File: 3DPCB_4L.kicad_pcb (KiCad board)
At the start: 4 copper layers, 100 x 60 mm, 777 parts, among them IC1 A5984_LP, IC2 A5984_LP, IC3 A5984_LP, IC4 A5984_LP, IC5 A5984_LP, IC6 MP9943, J10 , J11 , J12 , J13 , J14 , J15 , J16 , J2 , J3 , J4 , J5 , J6 , J7 , J8 , J9 , K1 CONN_3, K2 CONN_3, K3 CONN_3, K4 CONN_3, K5 CONN_3, K6 CONN_3, K7 CONN_3, K8 CONN_3, K9 CONN_3, P1 CONN_8, P11 CONN_3X2, P12 CONN_3X2, P13 CONN_4, P2 CONN_8, P5 CONN_4, P6 CONN_4, P7 CONN_4, P8 CONN_02X03, P9 CONN_4, U1 CONN_4_LERCHE, U10 MICRO-SD, U11 TC4427, U12 MCP4728, U13 CONN_4_LERCHE, U15 SPST_MOMENTARY, U16 CONN_4_LERCHE, U2 SPST_MOMENTARY, U21 CONN_4_LERCHE, U22 CONN_4_LERCHE, U23 MCP4728, U24 IRFH5302, U25 CONN_4_LERCHE, U3 BSS84, U4 CONN_4_LERCHE, U5 IRFH5302, U6 LPC1768_TQFP100, U7 IRFH5302, U8 IRFH5302, U9 TC4427

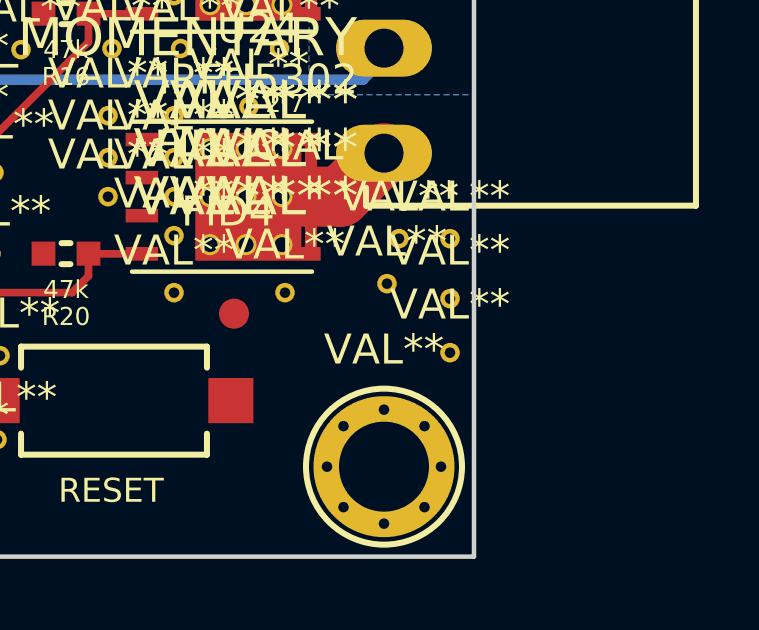
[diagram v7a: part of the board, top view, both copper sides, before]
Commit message: Spokes on high current path removed.
Spokes on high current path removed.
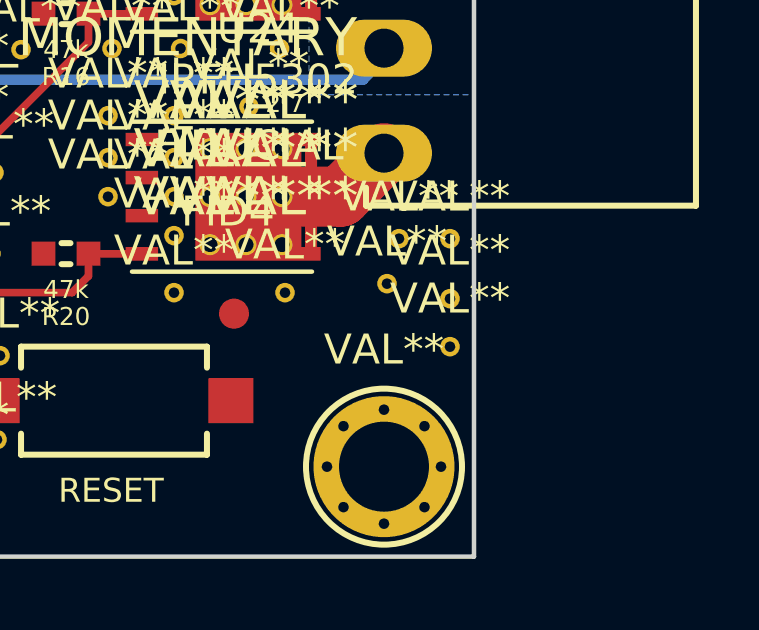
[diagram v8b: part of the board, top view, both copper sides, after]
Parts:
- moved ? 0.20 mm to (229.2, 188.5)
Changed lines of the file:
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@@
     (links 1072)
     (no_connects 0)
-    (area 129.924999 135.424999 230.075001 195.575001)
+    (area 126.046317 131.0284 237.651491 200.475)
     (thickness 1.6)
     (drawings 131)
@@
   (layers
     (0 F.Cu mixed)
-    (1 Inner2.Cu power)
-    (2 Inner1.Cu power)
+    (1 Inner2.Cu power hide)
+    (2 Inner1.Cu power hide)
     (31 B.Cu mixed)
     (32 B.Adhes user)
@@
     (mod_text_size 1 1)
     (mod_text_width 0.15)
-    (pad_size 4.32 3)
+    (pad_size 1.25 1.8)
     (pad_drill 0)
     (pad_to_mask_clearance 0)
@@
   )
   (module Lerche_via_0.35_GND (layer F.Cu)
-    (at 229.2 188.7)
+    (at 229.2 188.5)
     (fp_text reference "" (at 0 -3.2) (layer F.SilkS)
       (effects (font (size 1 1) (thickness 0.15)))
@@
       (net 171 "Net-(IC1-Pad17)"))
     (pad 2 smd rect (at 1.4 0) (size 1.25 1.8) (layers F.Cu F.Paste F.Mask)
-      (net 19 GND))
+      (net 19 GND) (zone_connect 2))
     (model Resistors_SMD.3dshapes/R_1206.wrl
       (at (xyz 0 0 0))
@@
       (net 173 "Net-(IC1-Pad20)"))
     (pad 2 smd rect (at 1.4 0 180) (size 1.25 1.8) (layers F.Cu F.Paste F.Mask)
-      (net 19 GND))
+      (net 19 GND) (zone_connect 2))
     (model Resistors_SMD.3dshapes/R_1206.wrl
       (at (xyz 0 0 0))
@@
       (net 195 "Net-(IC5-Pad17)"))
     (pad 2 smd rect (at 1.4 0) (size 1.25 1.8) (layers F.Cu F.Paste F.Mask)
-      (net 19 GND))
+      (net 19 GND) (zone_connect 2))
     (model Resistors_SMD.3dshapes/R_1206.wrl
       (at (xyz 0 0 0))
@@
       (net 197 "Net-(IC5-Pad20)"))
     (pad 2 smd rect (at 1.4 0 180) (size 1.25 1.8) (layers F.Cu F.Paste F.Mask)
-      (net 19 GND))
+      (net 19 GND) (zone_connect 2))
     (model Resistors_SMD.3dshapes/R_1206.wrl
       (at (xyz 0 0 0))
@@
       (net 189 "Net-(IC4-Pad17)"))
     (pad 2 smd rect (at 1.4 0) (size 1.25 1.8) (layers F.Cu F.Paste F.Mask)
-      (net 19 GND))
+      (net 19 GND) (zone_connect 2))
     (model Resistors_SMD.3dshapes/R_1206.wrl
       (at (xyz 0 0 0))
@@
       (net 183 "Net-(IC3-Pad17)"))
     (pad 2 smd rect (at 1.4 0) (size 1.25 1.8) (layers F.Cu F.Paste F.Mask)
-      (net 19 GND))
+      (net 19 GND) (zone_connect 2))
     (model Resistors_SMD.3dshapes/R_1206.wrl
       (at (xyz 0 0 0))
@@
       (net 177 "Net-(IC2-Pad17)"))
     (pad 2 smd rect (at 1.4 0) (size 1.25 1.8) (layers F.Cu F.Paste F.Mask)
-      (net 19 GND))
+      (net 19 GND) (zone_connect 2))
     (model Resistors_SMD.3dshapes/R_1206.wrl
       (at (xyz 0 0 0))
@@
       (net 191 "Net-(IC4-Pad20)"))
     (pad 2 smd rect (at 1.4 0 180) (size 1.25 1.8) (layers F.Cu F.Paste F.Mask)
-      (net 19 GND))
+      (net 19 GND) (zone_connect 2))
     (model Resistors_SMD.3dshapes/R_1206.wrl
       (at (xyz 0 0 0))
@@
       (net 185 "Net-(IC3-Pad20)"))
     (pad 2 smd rect (at 1.4 0 180) (size 1.25 1.8) (layers F.Cu F.Paste F.Mask)
-      (net 19 GND))
+      (net 19 GND) (zone_connect 2))
     (model Resistors_SMD.3dshapes/R_1206.wrl
       (at (xyz 0 0 0))
@@
       (net 179 "Net-(IC2-Pad20)"))
     (pad 2 smd rect (at 1.4 0 180) (size 1.25 1.8) (layers F.Cu F.Paste F.Mask)
-      (net 19 GND))
+      (net 19 GND) (zone_connect 2))
     (model Resistors_SMD.3dshapes/R_1206.wrl
       (at (xyz 0 0 0))
@@
     (polygon
       (pts
-        (xy 136 195.5) (xy 130 195.5) (xy 130 189.5) (xy 136 189.5)
-      )
-    )
-  )
-  (zone (net 0) (net_name "") (layer B.Cu) (hatch edge 0.508)
-    (connect_pads (clearance 0.2))
-    (min_thickness 0.2)
-    (keepout (tracks allowed) (vias allowed) (copperpour not_allowed))
-    (fill (arc_segments 16) (thermal_gap 0.254) (thermal_bridge_width 0.254))
-    (polygon
-      (pts
-        (xy 136 195.5) (xy 130 195.5) (xy 130 189.5) (xy 136 189.5)
-      )
-    )
-  )
-  (zone (net 0) (net_name "") (layer F.Cu) (hatch edge 0.508)
-    (connect_pads (clearance 0.2))
-    (min_thickness 0.2)
-    (keepout (tracks allowed) (vias allowed) (copperpour not_allowed))
-    (fill (arc_segments 16) (thermal_gap 0.254) (thermal_bridge_width 0.254))
-    (polygon
-      (pts
-        (xy 136 141.5) (xy 130 141.5) (xy 130 135.5) (xy 136 135.5)
+        (xy 136.5 195.5) (xy 130 195.5) (xy 130 189) (xy 136.5 189)
       )
     )
@@
     (polygon
       (pts
-        (xy 136 141.5) (xy 130 141.5) (xy 130 135.5) (xy 136 135.5)
+        (xy 136.5 195.5) (xy 130 195.5) (xy 130 189) (xy 136.5 189)
       )
     )
@@
     (polygon
       (pts
-        (xy 230 195.5) (xy 224 195.5) (xy 224 189.5) (xy 230 189.5)
+        (xy 136.5 142) (xy 130 142) (xy 130 135.5) (xy 136.5 135.5)
       )
     )
@@
     (polygon
       (pts
-        (xy 230 195.5) (xy 224 195.5) (xy 224 189.5) (xy 230 189.5)
+        (xy 136.5 142) (xy 130 142) (xy 130 135.5) (xy 136.5 135.5)
       )
     )
@@
     (polygon
       (pts
-        (xy 230 142) (xy 223.5 142) (xy 223.5 135.5) (xy 230 135.5)
+        (xy 230 195.5) (xy 223.5 195.5) (xy 223.5 189) (xy 230 189)
       )
     )
@@
     (polygon
       (pts
-        (xy 230 141.5) (xy 224 141.5) (xy 224 135.5) (xy 230 135.5)
+        (xy 230 195.5) (xy 223.5 195.5) (xy 223.5 189) (xy 230 189)
       )
     )
@@
     (polygon
       (pts
-        (xy 136 141.5) (xy 130 141.5) (xy 130 135.5) (xy 136 135.5)
-      )
-    )
-  )
-  (zone (net 0) (net_name "") (layer Inner1.Cu) (hatch edge 0.508)
-    (connect_pads (clearance 0.2))
-    (min_thickness 0.2)
-    (keepout (tracks allowed) (vias allowed) (copperpour not_allowed))
-    (fill (arc_segments 16) (thermal_gap 0.254) (thermal_bridge_width 0.254))
-    (polygon
-      (pts
-        (xy 136 141.5) (xy 130 141.5) (xy 130 135.5) (xy 136 135.5)
-      )
-    )
-  )
-  (zone (net 0) (net_name "") (layer Inner2.Cu) (hatch edge 0.508)
-    (connect_pads (clearance 0.2))
-    (min_thickness 0.2)
-    (keepout (tracks allowed) (vias allowed) (copperpour not_allowed))
-    (fill (arc_segments 16) (thermal_gap 0.254) (thermal_bridge_width 0.254))
-    (polygon
-      (pts
-        (xy 136 195.5) (xy 130 195.5) (xy 130 189.5) (xy 136 189.5)
+        (xy 136.5 142) (xy 130 142) (xy 130 135.5) (xy 136.5 135.5)
       )
     )
@@
     (polygon
       (pts
-        (xy 136 195.5) (xy 130 195.5) (xy 130 189.5) (xy 136 189.5)
+        (xy 136.5 142) (xy 130 142) (xy 130 135.5) (xy 136.5 135.5)
       )
     )
@@
     (polygon
       (pts
-        (xy 230 195.5) (xy 224 195.5) (xy 224 189.5) (xy 230 189.5)
+        (xy 136.5 195.5) (xy 130 195.5) (xy 130 189) (xy 136.5 189)
       )
     )
@@
     (polygon
       (pts
-        (xy 230 195.5) (xy 224 195.5) (xy 224 189.5) (xy 230 189.5)
+        (xy 136.5 195.5) (xy 130 195.5) (xy 130 189) (xy 136.5 189)
       )
     )
@@
     (polygon
       (pts
-        (xy 230 141.5) (xy 224 141.5) (xy 224 135.5) (xy 230 135.5)
+        (xy 230 195.5) (xy 223.5 195.5) (xy 223.5 189) (xy 230 189)
       )
     )
@@
     (polygon
       (pts
-        (xy 230 141.5) (xy 224 141.5) (xy 224 135.5) (xy 230 135.5)
+        (xy 230 195.5) (xy 223.5 195.5) (xy 223.5 189) (xy 230 189)
       )
     )
@@
     )
   )
-  (zone (net 0) (net_name "") (layer B.Cu) (hatch edge 0.508)
+  (zone (net 0) (net_name "") (layer F.Cu) (hatch edge 0.508)
     (connect_pads (clearance 0.16))
     (min_thickness 0.254)
@@
     (polygon
       (pts
-        (xy 223.5 135.5) (xy 230 135.5) (xy 230 142) (xy 223.5 142)
+        (xy 230 135.5) (xy 223.5 135.5) (xy 223.5 142) (xy 230 142)
       )
     )
@@
     (polygon
       (pts
-        (xy 223.506027 135.5) (xy 230.006027 135.5) (xy 230.006027 142) (xy 223.506027 142)
+        (xy 230 135.5) (xy 223.5 135.5) (xy 223.5 142) (xy 230 142)
       )
     )
@@
     (polygon
       (pts
-        (xy 223.5 135.5) (xy 230 135.5) (xy 230 142) (xy 223.5 142)
+        (xy 230 135.5) (xy 223.5 135.5) (xy 223.5 142) (xy 230 142)
+      )
+    )
+  )
+  (zone (net 0) (net_name "") (layer B.Cu) (hatch edge 0.508)
+    (connect_pads (clearance 0.16))
+    (min_thickness 0.254)
+    (keepout (tracks allowed) (vias allowed) (copperpour not_allowed))
+    (fill (arc_segments 16) (thermal_gap 0.508) (thermal_bridge_width 0.508))
+    (polygon
+      (pts
+        (xy 230 135.5) (xy 223.5 135.5) (xy 223.5 142) (xy 230 142)
       )
     )
